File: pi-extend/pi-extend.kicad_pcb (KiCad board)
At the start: 2 copper layers, 58.4 x 67.1 mm, 7 parts, among them J1 Conn_02x20_Odd_Even, J2 Conn_01x20_Male, J3 Conn_01x20_Male, J4 Conn_01x02_Male, J5 Conn_01x02_Male, J6 Conn_01x02_Male, J7 Conn_01x02_Male

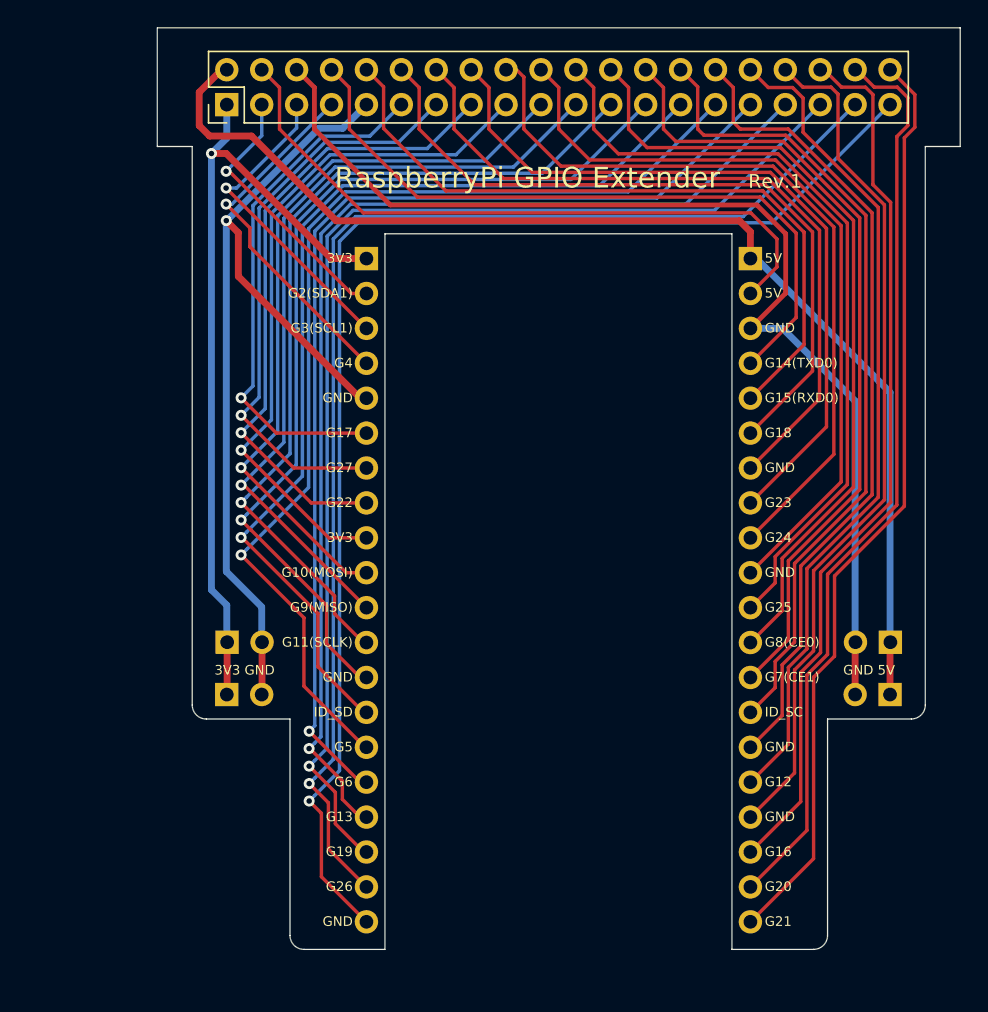
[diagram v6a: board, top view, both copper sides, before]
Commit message: [pi-extend] 5V 단자 위치 조정
Signed-off-by: Ju, Gyeong-min <jcmh74@gmail.com>
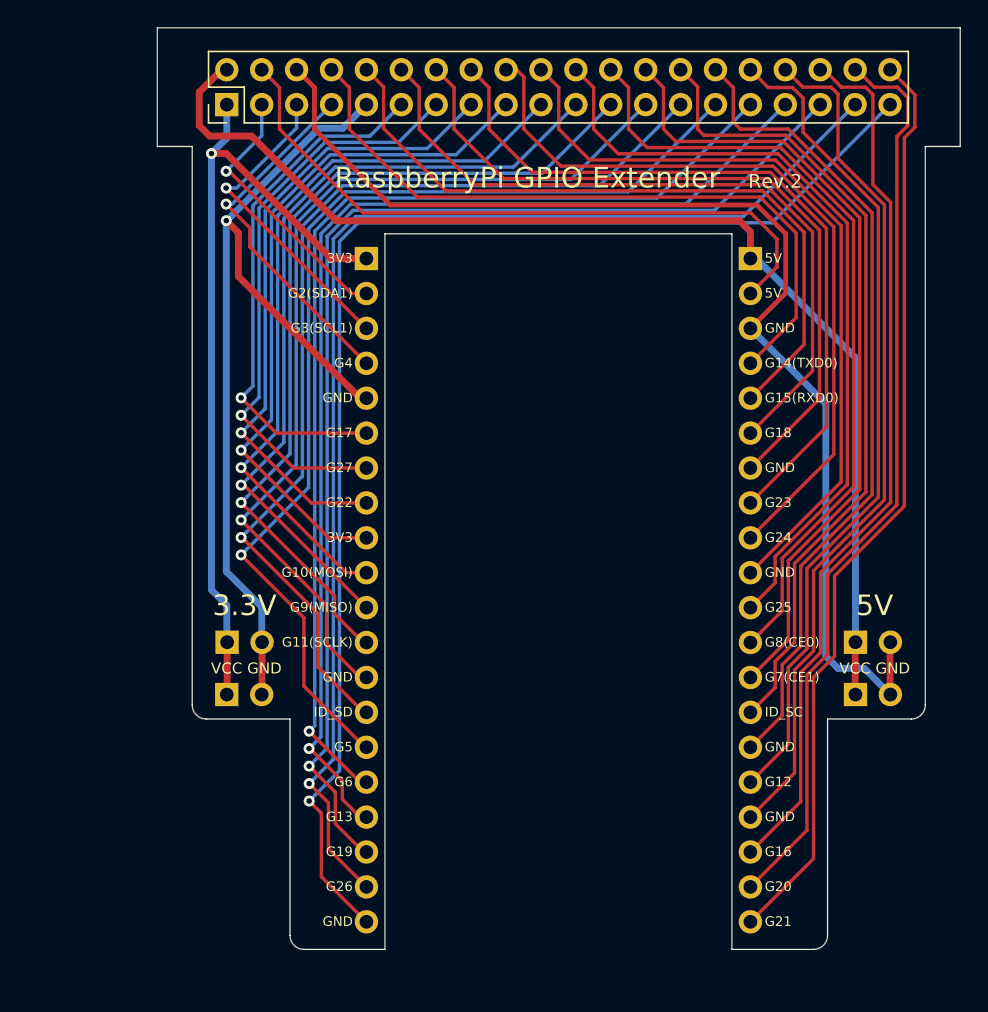
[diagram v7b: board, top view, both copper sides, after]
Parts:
- moved J7 2.54 mm to (184.4, 106.7), turned to 270 degrees
- moved J5 2.51 mm to (184.4, 110.5), turned to 270 degrees
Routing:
- net Net-(J1-Pad6): track 81.4 -> 86.0 mm
- net Net-(J1-Pad2): track 86.6 -> 85.5 mm
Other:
- board text added: "3.3V"
- board text added: "Rev.2"
- board text added: "VCC GND"
- board text removed: "3V3 GND"
- board text removed: "GND 5V"
- board text removed: "Rev.1"

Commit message: [pi-extend] rev3 초기안
Signed-off-by: Ju, Gyeong-min <jcmh74@gmail.com>
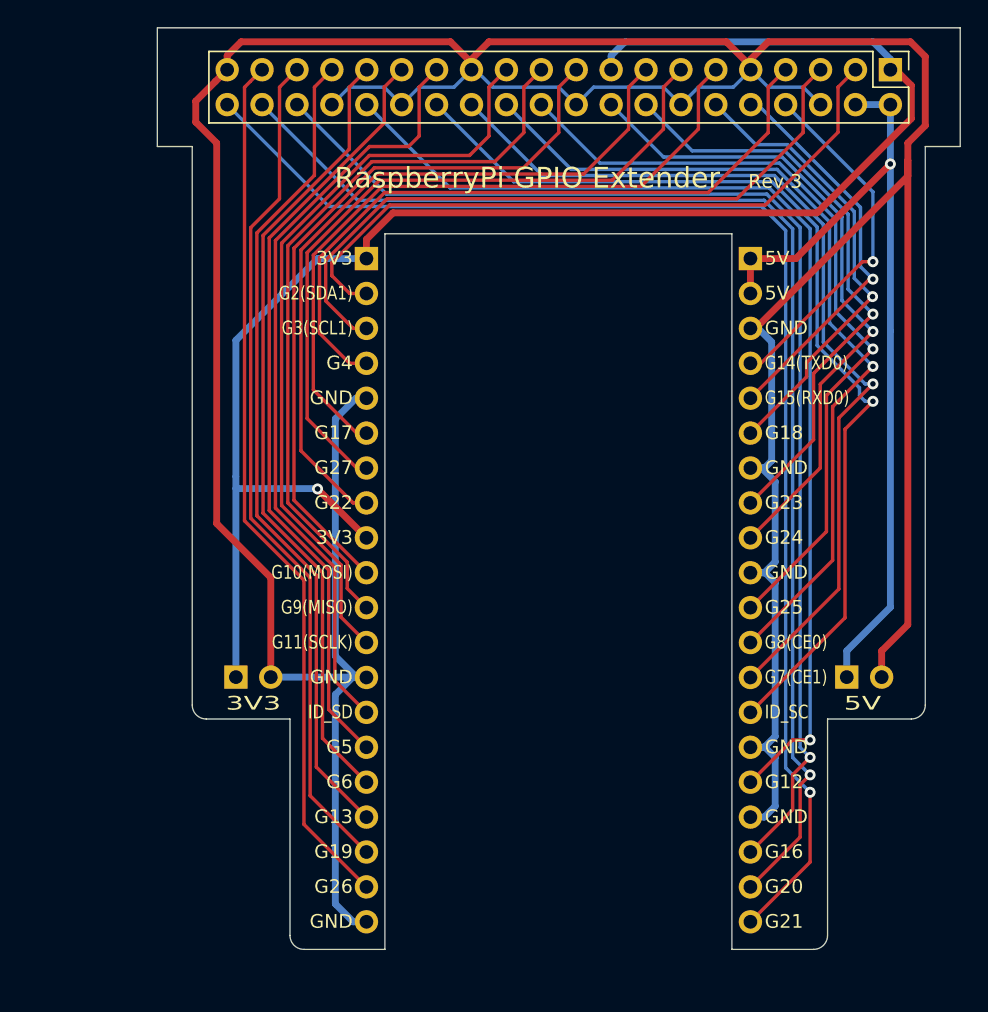
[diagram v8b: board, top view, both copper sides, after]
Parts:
- removed J6, J7: Conn_01x02_Male, Connector_PinHeader_2.54mm:PinHeader_1x02_P2.54mm_Vertical
- moved J1 48.4 mm to (186.9, 65.0), turned to 270 degrees
- moved J4 1.43 mm to (139.3, 109.2)
- moved J5 1.42 mm to (183.8, 109.2)
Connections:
- J1 pad 1: Net-(J1-Pad1) -> +3V3
- J1 pad 14: Net-(J1-Pad14) -> GND
- J1 pad 17: Net-(J1-Pad17) -> +3V3
- J1 pad 2: Net-(J1-Pad2) -> +5V
- J1 pad 20: Net-(J1-Pad20) -> GND
- J1 pad 25: Net-(J1-Pad25) -> GND
- J1 pad 30: Net-(J1-Pad30) -> GND
- J1 pad 34: Net-(J1-Pad34) -> GND
- J1 pad 39: Net-(J1-Pad39) -> GND
- J1 pad 4: Net-(J1-Pad4) -> +5V
- J1 pad 6: Net-(J1-Pad6) -> GND
- J1 pad 9: Net-(J1-Pad9) -> GND
- J2 pad 1: Net-(J1-Pad1) -> +3V3
- J2 pad 13: Net-(J1-Pad25) -> GND
- J2 pad 20: Net-(J1-Pad39) -> GND
- J2 pad 5: Net-(J1-Pad9) -> GND
- J2 pad 9: Net-(J1-Pad17) -> +3V3
- J3 pad 1: Net-(J1-Pad2) -> +5V
- J3 pad 10: Net-(J1-Pad20) -> GND
- J3 pad 15: Net-(J1-Pad30) -> GND
- J3 pad 17: Net-(J1-Pad34) -> GND
- J3 pad 2: Net-(J1-Pad4) -> +5V
- J3 pad 3: Net-(J1-Pad6) -> GND
- J3 pad 7: Net-(J1-Pad14) -> GND
- J4 pad 1: Net-(J1-Pad1) -> +3V3
- J4 pad 2: Net-(J1-Pad9) -> GND
- J5 pad 1: Net-(J1-Pad2) -> +5V
- J5 pad 2: Net-(J1-Pad6) -> GND
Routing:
- net GND: track 0.00 -> 306.9 mm
- net +3V3: track 0.00 -> 119.6 mm, vias 0 -> 1
- net Net-(J1-Pad39): track 96.3 -> 0.00 mm, vias 1 -> 0
- net Net-(J1-Pad6): track 86.0 -> 0.00 mm
- net Net-(J1-Pad2): track 85.5 -> 0.00 mm
- net Net-(J1-Pad25): track 67.7 -> 0.00 mm, vias 1 -> 0
- net Net-(J1-Pad9): track 66.7 -> 0.00 mm, vias 1 -> 0
- net Net-(J1-Pad34): track 62.6 -> 0.00 mm
- net +5V: track 0.00 -> 61.1 mm, vias 0 -> 1
- net Net-(J1-Pad30): track 59.7 -> 0.00 mm
- net Net-(J1-Pad1): track 58.3 -> 0.00 mm, vias 1 -> 0
- net Net-(J1-Pad20): track 56.3 -> 0.00 mm
- net Net-(J1-Pad14): track 53.9 -> 0.00 mm
- net Net-(J1-Pad17): track 50.3 -> 0.00 mm, vias 1 -> 0
- net Net-(J1-Pad4): track 49.1 -> 0.00 mm
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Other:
- board text added: "Rev.3"
- board text removed: "3.3V"
- board text removed: "Rev.2"
- board text removed: "Select suitable pin for Breadboard"
- board text removed: "VCC GND"
